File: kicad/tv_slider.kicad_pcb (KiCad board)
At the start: 2 copper layers, 131.5 x 79.5 mm, 96 parts, among them J1 MC 1,5/2-G-3.81, J2 MC 1,5/6-G-3.81, J3 MC 1,5/4-G-3.81, J4 MC 1,5/3-G-3.81, J5 MC 1,5/3-G-3.81, J6 MC 1,5/3-G-3.81, J7 MC 1,5/3-G-3.81, J8 Conn_01x04, Q1 CSD19537Q3, Q2 BSS138, U1 TPS26632RGE, U2 LMR33610ADDAR, U3 LMR33610ADDAR, U4 ESP32-C6-DEVKITC-1-N8, U5 DRV8452DDWR, U6 ISL3280ExHZ, U7 LS7184N-S, U8 ISL3280ExHZ

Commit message: Completed the PCB design. Ready for final review.
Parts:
- removed R6: 100k, Resistor_SMD:R_0603_1608Metric
- removed U5: DRV8452DDWR, local_library:IC_DRV8452DDWR
- added U9: DRV8452SPWPR, local_library:IC_DRV8452SPWPR, F.Cu at (168.1, 87.0)
- C21, C22: value 150u -> 100u; footprint Capacitor_SMD:CP_Elec_10x12.5 -> Capacitor_SMD:CP_Elec_8x11.9
- D1: value 1.5SMC33CA -> SMBJ33CA; footprint Diode_SMD:D_SMC -> Diode_SMD:D_SMB
- moved C21 70.9 mm to (145.3, 62.5), turned to 180 degrees
- moved C8 61.2 mm to (153.9, 120.4), turned to 90 degrees
- moved C7 58.1 mm to (150.9, 120.4), turned to 90 degrees
- moved C22 51.3 mm to (145.3, 72.1), turned to 180 degrees
- moved C15 46.4 mm to (168.7, 94.1), turned to 0 degrees
- moved R2 45.3 mm to (139.7, 111.8), turned to -90 degrees
- moved C16 43.6 mm to (162.6, 90.4)
- moved C11 43.3 mm to (138.7, 94.0), turned to 180 degrees
- moved R3 43.1 mm to (142.7, 112.3)
- moved J3 42.6 mm to (177.8, 92.5)
- moved C18 41.5 mm to (164.1, 79.8), turned to 180 degrees
- moved C36 41.4 mm to (158.0, 117.9), turned to 180 degrees
- moved C35 39.0 mm to (162.1, 117.9), turned to 180 degrees
- moved D8 38.9 mm to (172.7, 125.5)
- moved C33 38.7 mm to (169.2, 125.5)
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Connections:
- C12 pad 1: +3.3V -> +3V3
- C13 pad 1: +3.3V -> +3V3
- J3 pad 1: /Motor drive/B- -> /Motor drive/A+
- J3 pad 2: /Motor drive/B+ -> /Motor drive/A-
- J3 pad 3: /Motor drive/A- -> /Motor drive/B-
- J3 pad 4: /Motor drive/A+ -> /Motor drive/B+
- L2 pad 2: +3.3V -> +3V3
- R4 pad 1: +3.3V -> +3V3
- U4 pad J1_10: unconnected-(U4-GPIO10-PadJ1_10) -> /MCU/MOSI
- U4 pad J1_11: unconnected-(U4-GPIO11-PadJ1_11) -> /MCU/MISO
- U4 pad J1_12: unconnected-(U4-GPIO2-PadJ1_12) -> /MCU/~{CS}
- U4 pad J1_13: unconnected-(U4-GPIO3-PadJ1_13) -> /MCU/~{FAULT}
- U4 pad J1_2: unconnected-(U4-CHIP_PU-PadJ1_2) -> /MCU/COUNT
- U4 pad J1_3: unconnected-(U4-GPIO4-PadJ1_3) -> /MCU/UP/~{DOWN}
- U4 pad J1_5: unconnected-(U4-GPIO6-PadJ1_5) -> /MCU/~{SLEEP}
- U4 pad J1_6: unconnected-(U4-GPIO7-PadJ1_6) -> /MCU/ENABLE
- U4 pad J1_7: unconnected-(U4-GPIO0-PadJ1_7) -> /MCU/DIR
- U4 pad J1_8: unconnected-(U4-GPIO1-PadJ1_8) -> /MCU/STEP
- U4 pad J1_9: unconnected-(U4-GPIO8-PadJ1_9) -> /MCU/SCLK
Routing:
- net +5V: track 58.6 -> 173.1 mm, vias 0 -> 4
- net +3V3: track 43.2 -> 152.8 mm, vias 0 -> 8
- net /MCU/~{SLEEP}: track 0.00 -> 46.0 mm, vias 0 -> 2
- net GND: track 34.4 -> 80.0 mm, vias 5 -> 49
- net Net-(U2-EN): track 0.00 -> 44.8 mm
- net /MCU/ENABLE: track 0.00 -> 43.1 mm, vias 0 -> 2
- net /MCU/DIR: track 0.00 -> 41.1 mm, vias 0 -> 2
- net /MCU/STEP: track 0.00 -> 39.7 mm
- net /MCU/~{FAULT}: track 0.00 -> 39.3 mm
- net /MCU/~{CS}: track 0.00 -> 38.8 mm, vias 0 -> 2
- net /MCU/SCLK: track 0.00 -> 38.7 mm
- net /MCU/MISO: track 0.00 -> 38.3 mm
- net /MCU/MOSI: track 0.00 -> 37.7 mm
- net /MCU/UP/~{DOWN}: track 0.00 -> 36.5 mm, vias 0 -> 4
- net /MCU/COUNT: track 0.00 -> 33.6 mm, vias 0 -> 4
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- added copper zone on F.Cu, net +3V3
- added copper zone on F.Cu, net +5V
- added copper zone on F.Cu, net /Motor drive/A+
- added copper zone on F.Cu, net /Motor drive/A-
- added copper zone on F.Cu, net /Motor drive/B+
- added copper zone on F.Cu, net /Motor drive/B-
- added copper zone on F.Cu, net /Power supply/Vin
- added copper zone on F.Cu, net GND
- added copper zone on F.Cu, net Net-(Q1-D)
- added copper zone on F.Cu, net Net-(U2-FB)
- added copper zone on F.Cu, net Net-(U2-SW)
- added copper zone on F.Cu, net Net-(U3-FB)
- added copper zone on F.Cu, net Net-(U3-SW)
- added copper zone on F.Cu, net Vdrive
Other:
- board size 131.5 x 79.5 mm -> 102.6 x 75.2 mm
- board text added: "TV-Slider - 1.0 Copyright (c) 2025"

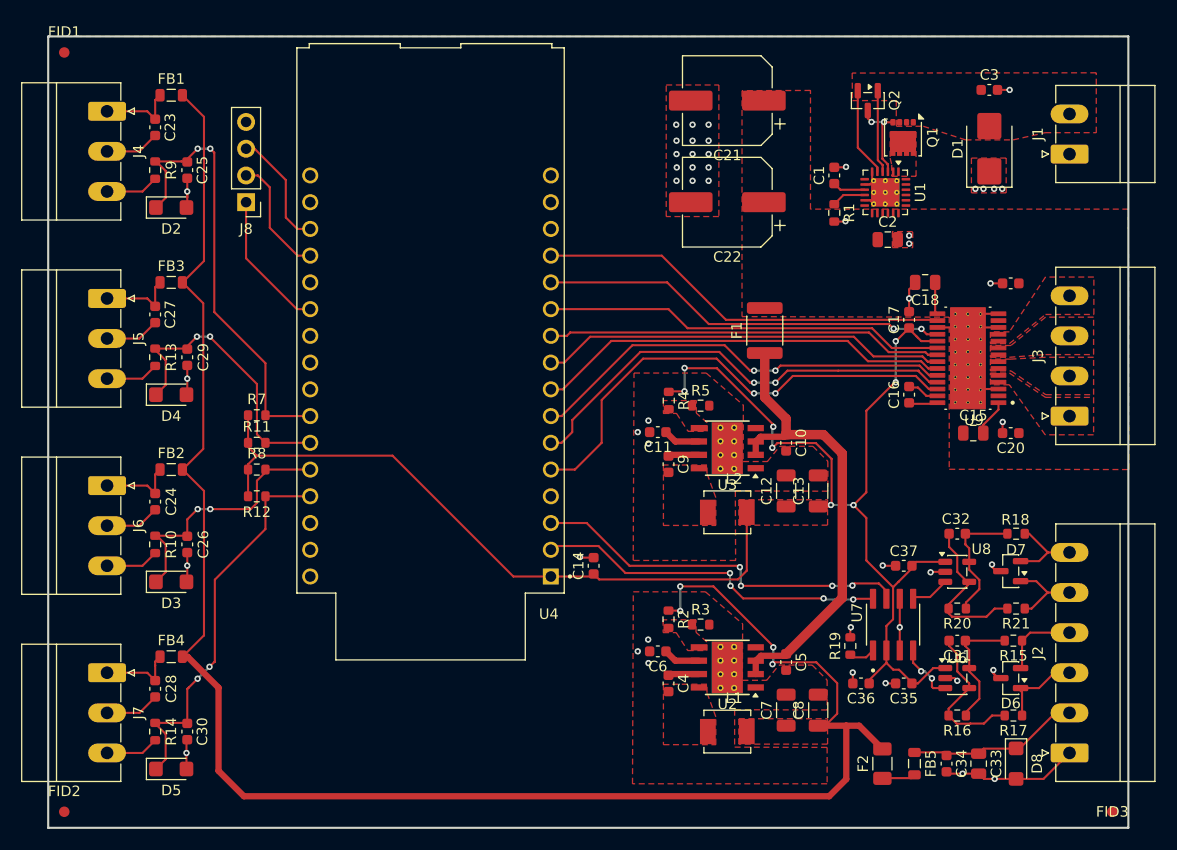
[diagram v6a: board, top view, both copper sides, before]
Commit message: Reviewed the part numbers, footprints and pin numbers.
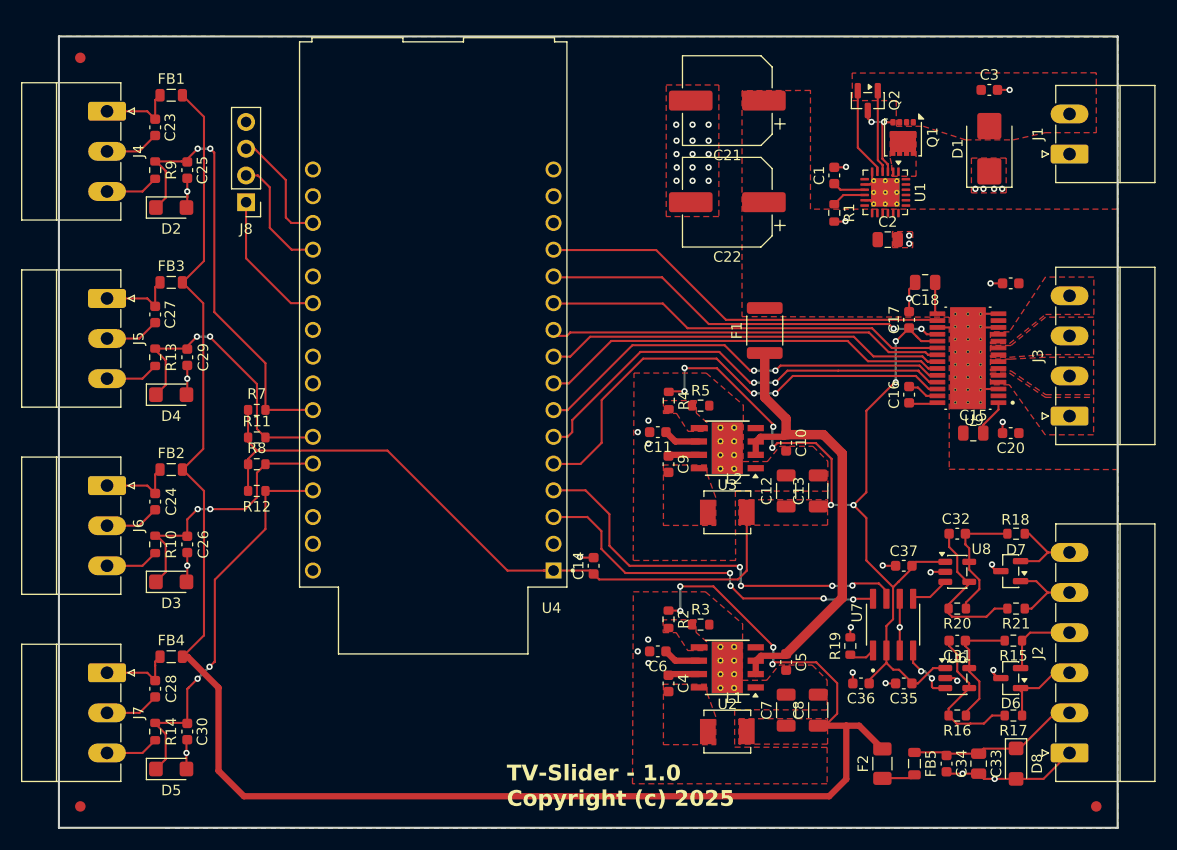
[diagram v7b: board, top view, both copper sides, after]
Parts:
- F2: value 0.2A -> 200mA
- moved FID3 1.61 mm to (180.3, 129.5)
- moved FID2 1.61 mm to (83.8, 129.5)
- moved FID1 1.61 mm to (83.8, 58.4)
- moved U4 0.62 mm to (117.3, 82.8)
- moved R11 0.51 mm to (100.6, 94.5)
- moved R12 0.51 mm to (100.6, 99.6)
- moved R7 0.51 mm to (100.6, 91.9)
- moved R8 0.51 mm to (100.6, 97.0)
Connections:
- U4 pad J1_2: /MCU/COUNT -> unconnected-(U4-CHIP_PU-PadJ1_2)
- U4 pad J1_3: /MCU/UP/~{DOWN} -> /MCU/COUNT
- U4 pad J1_4: unconnected-(U4-GPIO5-PadJ1_4) -> /MCU/UP/~{DOWN}
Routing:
- net /MCU/UP/~{DOWN}: track 36.5 -> 39.3 mm
- net /MCU/COUNT: track 33.6 -> 35.3 mm
- net +3V3: track 152.8 -> 153.6 mm
- net /MCU/SCLK: track 38.7 -> 37.9 mm
- net /MCU/DIR: track 41.1 -> 40.3 mm
- net /MCU/STEP: track 39.7 -> 38.9 mm
- net /MCU/ENABLE: track 43.1 -> 42.3 mm
- net /Location sensors/IN_SLOW: track 25.1 -> 25.9 mm
- net /MCU/~{SLEEP}: track 46.0 -> 45.3 mm
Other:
- board size 102.6 x 75.2 mm -> 100.6 x 75.2 mm
